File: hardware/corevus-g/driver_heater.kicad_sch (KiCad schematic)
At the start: 4 parts, among them J21 Screw_Terminal_01x02, Q26 60N03F

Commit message: test
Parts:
- R3: value 1kΩ -> 10kΩ
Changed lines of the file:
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@@
       (effects (font (size 0.8 0.8)) (justify right))
     )
-    (property "Value" "1kΩ" (at 63.5 71.12 90)
+    (property "Value" "10kΩ" (at 63.5 71.12 90)
       (effects (font (size 0.8 0.8)))
     )

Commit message: aonteuhasntoidanouidoenuthidntoehuid
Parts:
- Q26: symbol corevus:Q_NMOS-E_Generic_SSSGDDDD -> corevus:NMOS_DFN8
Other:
- moved on the sheet: D1, R3
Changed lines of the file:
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@@
 (kicad_sch (version 20230121) (generator eeschema)
   (paper "User" 140.005 148.006)
-  (junction (at 63.5 60.96) (diameter 0) (color 0 0 0 0)
-  )
-  (wire (pts (xy 63.5 60.96) (xy 63.5 62.23))
+  (junction (at 64.77 59.69) (diameter 0) (color 0 0 0 0)
+  )
+  (wire (pts (xy 64.77 59.69) (xy 64.77 60.96))
     (stroke (width 0) (type default))
   )
@@
     (stroke (width 0) (type default))
   )
-  (wire (pts (xy 63.5 68.58) (xy 63.5 67.31))
-    (stroke (width 0) (type default))
-  )
-  (wire (pts (xy 60.96 60.96) (xy 63.5 60.96))
-    (stroke (width 0) (type default))
-  )
-  (wire (pts (xy 63.5 60.96) (xy 71.12 60.96))
+  (wire (pts (xy 64.77 67.31) (xy 64.77 66.04))
+    (stroke (width 0) (type default))
+  )
+  (wire (pts (xy 62.23 59.69) (xy 64.77 59.69))
+    (stroke (width 0) (type default))
+  )
+  (wire (pts (xy 64.77 59.69) (xy 72.39 59.69))
     (stroke (width 0) (type default))
   )
@@
     (stroke (width 0) (type default))
   )
-  (wire (pts (xy 63.5 74.93) (xy 63.5 73.66))
+  (wire (pts (xy 64.77 73.66) (xy 64.77 72.39))
     (stroke (width 0) (type default))
   )
@@
     (effects (font (size 1.27 1.27)) (justify left bottom))
   )
-  (hierarchical_label "En" (shape input) (at 60.96 60.96 180) (fields_autoplaced)
+  (hierarchical_label "En" (shape input) (at 62.23 59.69 180) (fields_autoplaced)
     (effects (font (size 1.27 1.27)) (justify right))
   )
@@
     )
   )
-  (symbol (lib_id "Device:LED_Small") (at 63.5 64.77 90) (unit 1)
-    (in_bom yes) (on_board yes) (dnp no)
-    (property "Reference" "D1" (at 62.5 63.77 0)
+  (symbol (lib_id "Device:LED_Small") (at 64.77 63.5 90) (unit 1)
+    (in_bom yes) (on_board yes) (dnp no)
+    (property "Reference" "D1" (at 63.77 62.5 0)
       (effects (font (size 0.8 0.8)) (justify left))
     )
-    (property "Value" "Red" (at 62.5 65.77 0)
+    (property "Value" "Red" (at 63.77 64.5 0)
       (effects (font (size 0.8 0.8)) (justify right))
     )
-    (property "Footprint" "AlphaLib:0402LED" (at 63.5 64.77 90)
-      (effects (font (size 1.27 1.27)) hide)
-    )
-    (property "Datasheet" "~" (at 63.5 64.77 90)
+    (property "Footprint" "AlphaLib:0402LED" (at 64.77 63.5 90)
+      (effects (font (size 1.27 1.27)) hide)
+    )
+    (property "Datasheet" "~" (at 64.77 63.5 90)
       (effects (font (size 1.27 1.27)) hide)
     )
@@
     )
   )
-  (symbol (lib_id "power:GND") (at 63.5 74.93 0) (unit 1)
-    (in_bom yes) (on_board yes) (dnp no)
-    (property "Reference" "#PWR0161" (at 63.5 81.28 0)
-      (effects (font (size 1.27 1.27)) hide)
-    )
-    (property "Value" "GND" (at 63.5 77.47 90)
+  (symbol (lib_id "power:GND") (at 64.77 73.66 0) (unit 1)
+    (in_bom yes) (on_board yes) (dnp no)
+    (property "Reference" "#PWR0161" (at 64.77 80.01 0)
+      (effects (font (size 1.27 1.27)) hide)
+    )
+    (property "Value" "GND" (at 64.77 76.2 90)
       (effects (font (size 1.27 1.27)) (justify right) hide)
     )
-    (property "Footprint" "" (at 63.5 74.93 0)
-      (effects (font (size 1.27 1.27)) hide)
-    )
-    (property "Datasheet" "" (at 63.5 74.93 0)
+    (property "Footprint" "" (at 64.77 73.66 0)
+      (effects (font (size 1.27 1.27)) hide)
+    )
+    (property "Datasheet" "" (at 64.77 73.66 0)
       (effects (font (size 1.27 1.27)) hide)
     )
@@
     )
   )
-  (symbol (lib_id "corevus:Q_NMOS-E_Generic_SSSGDDDD") (at 74.93 59.69 0) (unit 1)
-    (in_bom yes) (on_board yes) (dnp no)
-    (property "Reference" "Q26" (at 80.01 58.42 0)
-      (effects (font (size 1.27 1.27)) (justify left))
-    )
-    (property "Value" "60N03F" (at 80.01 60.96 0)
-      (effects (font (size 1.27 1.27)) (justify left))
-    )
-    (property "Footprint" "corevus:MOSFET_DFN8" (at 80.01 57.15 0)
-      (effects (font (size 1.27 1.27)) hide)
-    )
-    (property "Datasheet" "~" (at 74.93 59.69 0)
+  (symbol (lib_id "corevus:NMOS_DFN8") (at 76.2 59.69 0) (unit 1)
+    (in_bom yes) (on_board yes) (dnp no)
+    (property "Reference" "Q26" (at 81.28 58.42 0)
+      (effects (font (size 1.27 1.27)) (justify left))
+    )
+    (property "Value" "60N03F" (at 81.28 60.96 0)
+      (effects (font (size 1.27 1.27)) (justify left))
+    )
+    (property "Footprint" "corevus:MOSFET_DFN8" (at 76.2 76.2 0)
+      (effects (font (size 1.27 1.27)) hide)
+    )
+    (property "Datasheet" "~" (at 76.2 78.74 0)
       (effects (font (size 1.27 1.27)) hide)
     )
@@
     )
   )
-  (symbol (lib_id "Device:R_Small") (at 63.5 71.12 0) (mirror y) (unit 1)
-    (in_bom yes) (on_board yes) (dnp no)
-    (property "Reference" "R3" (at 62.5 73.39 90)
+  (symbol (lib_id "Device:R_Small") (at 64.77 69.85 0) (mirror y) (unit 1)
+    (in_bom yes) (on_board yes) (dnp no)
+    (property "Reference" "R3" (at 63.77 72.12 90)
       (effects (font (size 0.8 0.8)) (justify right))
     )
-    (property "Value" "10kΩ" (at 63.5 71.12 90)
+    (property "Value" "10kΩ" (at 64.77 69.85 90)
       (effects (font (size 0.8 0.8)))
     )
-    (property "Footprint" "AlphaLib:0402R" (at 63.5 71.12 0)
-      (effects (font (size 1.27 1.27)) hide)
-    )
-    (property "Datasheet" "~" (at 63.5 71.12 0)
-      (effects (font (size 1.27 1.27)) hide)
-    )
+    (property "Footprint" "AlphaLib:0402R" (at 64.77 69.85 0)
+      (effects (font (size 1.27 1.27)) hide)
+    )
+    (property "Datasheet" "~" (at 64.77 69.85 0)
+      (effects (font (size 1.27 1.27)) hide)
+    )

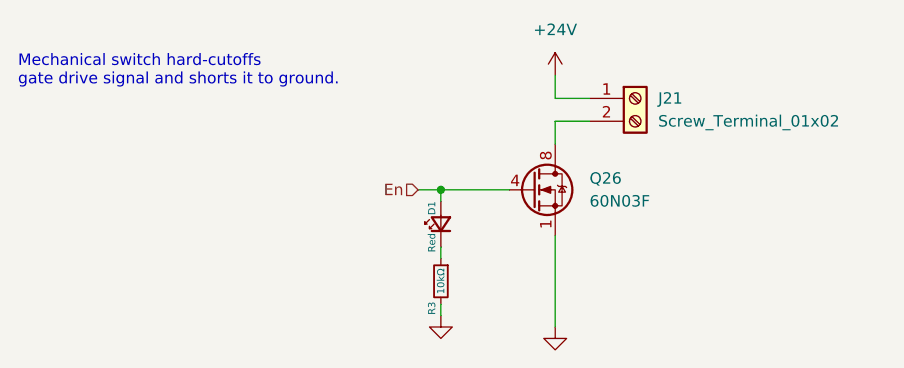
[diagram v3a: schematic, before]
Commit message: version control appears to have magically disappeared the single and dual 2160 driver files :(((((((((, but got some work done on CvG nonetheless
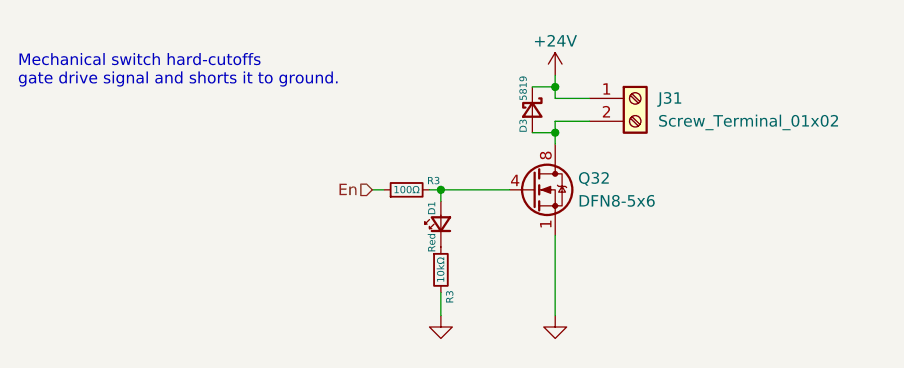
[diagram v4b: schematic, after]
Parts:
- added D3: 5819, Diode_SMD:D_SOD-123, symbol Device:D_Schottky_Small
- added R3: 100Ω, AlphaLib:0402R, symbol Device:R_Small
- J31: renamed from J21; footprint corevus:DB125-3.81-2P -> corevus:DB127V-5.0-2P
- Q32: renamed from Q26; value 60N03F -> DFN8-5x6; footprint corevus:MOSFET_DFN8 -> corevus:MOSFET_DFN8_5x6
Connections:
- net +24V: now also D3.1 (K)
- net En: now also R3.1; no longer D1.2 (A), Q32.4 (G)
- net at J31.2 (Pin_2), Q32.5 (D), Q32.6 (D)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: now also D3.2 (A)
- new net: D1.2 (A), Q32.4 (G), R3.2
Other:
- moved on the sheet: R3

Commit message: v0.4 mostly complete, board needs minor revisions (e.g. pin swap)
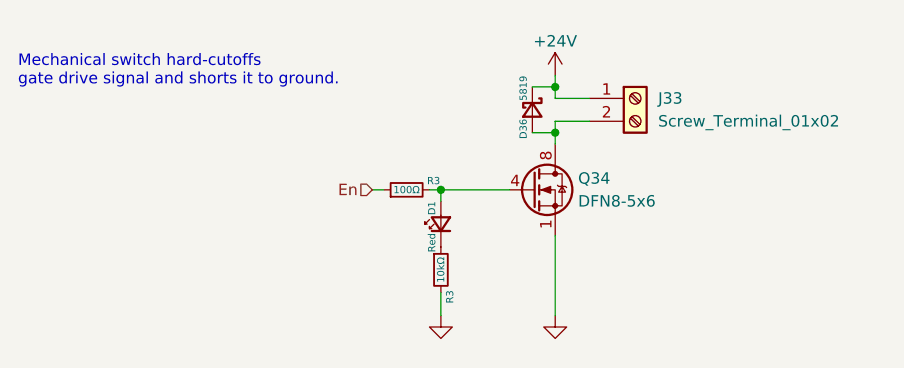
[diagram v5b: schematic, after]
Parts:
- renumbered D3 to D36, J31 to J33, Q32 to Q34
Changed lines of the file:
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@@
   (symbol (lib_id "Connector:Screw_Terminal_01x02") (at 86.36 49.53 0) (unit 1)
     (in_bom yes) (on_board yes) (dnp no)
-    (property "Reference" "J31" (at 88.9 49.53 0)
+    (property "Reference" "J33" (at 88.9 49.53 0)
       (effects (font (size 1.27 1.27)) (justify left))
     )
@@
     (instances
       (project "corevus-g"
-        (path "/1a565782-f217-442e-b118-196625f31c53/e431a135-0fb4-461f-9017-9bc2d88ea1f7"
-          (reference "J31") (unit 1)
-        )
         (path "/1a565782-f217-442e-b118-196625f31c53/a01cd58f-7f75-4e1a-8889-9711b3d0cced"
           (reference "J33") (unit 1)
@@
       )
       (project "corevus-g"
-        (path "/1a565782-f217-442e-b118-196625f31c53"
-          (reference "R76") (unit 1)
-        )
-        (path "/1a565782-f217-442e-b118-196625f31c53/e431a135-0fb4-461f-9017-9bc2d88ea1f7"
-          (reference "R121") (unit 1)
-        )
         (path "/1a565782-f217-442e-b118-196625f31c53/a01cd58f-7f75-4e1a-8889-9711b3d0cced"
           (reference "R123") (unit 1)
@@
   (symbol (lib_id "power:GND") (at 77.47 73.66 0) (unit 1)
     (in_bom yes) (on_board yes) (dnp no)
-    (property "Reference" "#PWR0118" (at 77.47 80.01 0)
+    (property "Reference" "#PWR065" (at 77.47 80.01 0)
       (effects (font (size 1.27 1.27)) hide)
     )
@@
     (instances
       (project "corevus-g"
-        (path "/1a565782-f217-442e-b118-196625f31c53"
-          (reference "#PWR0118") (unit 1)
-        )
-        (path "/1a565782-f217-442e-b118-196625f31c53/e431a135-0fb4-461f-9017-9bc2d88ea1f7"
-          (reference "#PWR050") (unit 1)
-        )
         (path "/1a565782-f217-442e-b118-196625f31c53/a01cd58f-7f75-4e1a-8889-9711b3d0cced"
           (reference "#PWR065") (unit 1)
@@
   (symbol (lib_id "power:+24V") (at 77.47 46.99 0) (unit 1)
     (in_bom yes) (on_board yes) (dnp no)
-    (property "Reference" "#PWR049" (at 77.47 50.8 0)
+    (property "Reference" "#PWR064" (at 77.47 50.8 0)
       (effects (font (size 1.27 1.27)) hide)
     )
@@
     (instances
       (project "corevus-g"
-        (path "/1a565782-f217-442e-b118-196625f31c53/e431a135-0fb4-461f-9017-9bc2d88ea1f7"
-          (reference "#PWR049") (unit 1)
-        )
         (path "/1a565782-f217-442e-b118-196625f31c53/a01cd58f-7f75-4e1a-8889-9711b3d0cced"
           (reference "#PWR064") (unit 1)
@@
       )
       (project "corevus-g"
-        (path "/1a565782-f217-442e-b118-196625f31c53"
-          (reference "D18") (unit 1)
-        )
-        (path "/1a565782-f217-442e-b118-196625f31c53/e431a135-0fb4-461f-9017-9bc2d88ea1f7"
-          (reference "D32") (unit 1)
-        )
         (path "/1a565782-f217-442e-b118-196625f31c53/a01cd58f-7f75-4e1a-8889-9711b3d0cced"
           (reference "D34") (unit 1)
@@
   (symbol (lib_id "Device:D_Schottky_Small") (at 74.93 50.8 270) (unit 1)
     (in_bom yes) (on_board yes) (dnp no)
-    (property "Reference" "D3" (at 73.93 51.8 0)
+    (property "Reference" "D36" (at 73.93 51.8 0)
       (effects (font (size 0.8 0.8)) (justify left))
     )
@@
     (instances
       (project "corevus-g"
-        (path "/1a565782-f217-442e-b118-196625f31c53"
-          (reference "D3") (unit 1)
-        )
         (path "/1a565782-f217-442e-b118-196625f31c53/bb16317b-ca89-4c54-91fa-fbae4a7551b1"
           (reference "D36") (unit 1)
         )
-        (path "/1a565782-f217-442e-b118-196625f31c53/e431a135-0fb4-461f-9017-9bc2d88ea1f7"
-          (reference "D37") (unit 1)
-        )
         (path "/1a565782-f217-442e-b118-196625f31c53/8e27c19c-e19c-4813-a1cf-aa58793105a1"
           (reference "D38") (unit 1)
@@
   (symbol (lib_id "power:GND") (at 64.77 73.66 0) (unit 1)
     (in_bom yes) (on_board yes) (dnp no)
-    (property "Reference" "#PWR0161" (at 64.77 80.01 0)
+    (property "Reference" "#PWR063" (at 64.77 80.01 0)
       (effects (font (size 1.27 1.27)) hide)
     )
@@
     (instances
       (project "corevus-g"
-        (path "/1a565782-f217-442e-b118-196625f31c53"
-          (reference "#PWR0161") (unit 1)
-        )
-        (path "/1a565782-f217-442e-b118-196625f31c53/e431a135-0fb4-461f-9017-9bc2d88ea1f7"
-          (reference "#PWR048") (unit 1)
-        )
         (path "/1a565782-f217-442e-b118-196625f31c53/a01cd58f-7f75-4e1a-8889-9711b3d0cced"
           (reference "#PWR063") (unit 1)
@@
   (symbol (lib_id "corevus:NMOS_DFN8") (at 76.2 59.69 0) (unit 1)
     (in_bom yes) (on_board yes) (dnp no)
-    (property "Reference" "Q32" (at 80.01 58.42 0)
+    (property "Reference" "Q34" (at 80.01 58.42 0)
       (effects (font (size 1.27 1.27)) (justify left))
     )
@@
     (instances
       (project "corevus-g"
-        (path "/1a565782-f217-442e-b118-196625f31c53/e431a135-0fb4-461f-9017-9bc2d88ea1f7"
-          (reference "Q32") (unit 1)
-        )
         (path "/1a565782-f217-442e-b118-196625f31c53/a01cd58f-7f75-4e1a-8889-9711b3d0cced"
           (reference "Q34") (unit 1)
@@
       )
       (project "corevus-g"
-        (path "/1a565782-f217-442e-b118-196625f31c53"
-          (reference "R76") (unit 1)
-        )
-        (path "/1a565782-f217-442e-b118-196625f31c53/e431a135-0fb4-461f-9017-9bc2d88ea1f7"
-          (reference "R114") (unit 1)
-        )
         (path "/1a565782-f217-442e-b118-196625f31c53/a01cd58f-7f75-4e1a-8889-9711b3d0cced"
           (reference "R116") (unit 1)

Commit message: non-working commit, moved around various connectors etc in preparation for v0.5
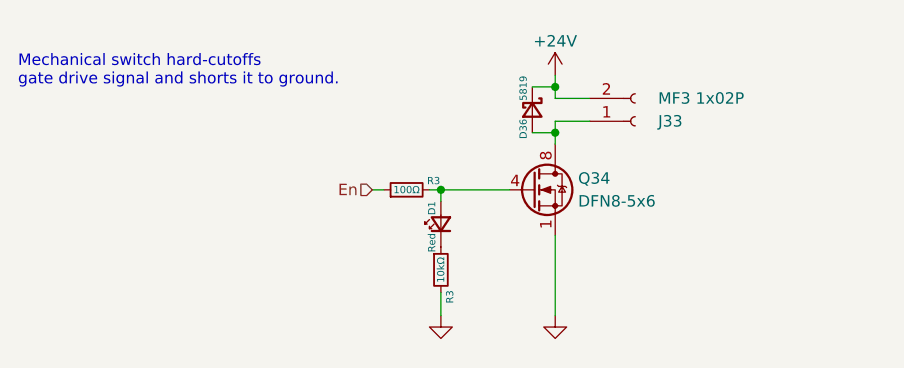
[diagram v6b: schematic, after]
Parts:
- J33: value Screw_Terminal_01x02 -> MF3 1x02P; footprint corevus:DB127V-5.0-2P -> corevus:XKB_X3025WR-02; symbol Connector:Screw_Terminal_01x02 -> Connector:Conn_01x02_Socket
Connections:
- net +24V: now also J33.2 (Pin_2); no longer J33.1 (Pin_1)
- net at D36.2 (A), Q34.5 (D), Q34.6 (D)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: now also J33.1 (Pin_1); no longer J33.2 (Pin_2)
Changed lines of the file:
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@@
     (effects (font (size 1.27 1.27)) (justify right))
   )
-  (symbol (lib_id "Connector:Screw_Terminal_01x02") (at 86.36 49.53 0) (unit 1)
+  (symbol (lib_id "Connector:Conn_01x02_Socket") (at 86.36 52.07 0) (mirror x) (unit 1)
     (in_bom yes) (on_board yes) (dnp no)
-    (property "Reference" "J33" (at 88.9 49.53 0)
+    (property "Reference" "J33" (at 88.9 52.07 0)
       (effects (font (size 1.27 1.27)) (justify left))
     )
-    (property "Value" "Screw_Terminal_01x02" (at 88.9 52.07 0)
+    (property "Value" "MF3 1x02P" (at 88.9 49.53 0)
       (effects (font (size 1.27 1.27)) (justify left))
     )
-    (property "Footprint" "corevus:DB127V-5.0-2P" (at 86.36 49.53 0)
+    (property "Footprint" "corevus:XKB_X3025WR-02" (at 86.36 52.07 0)
       (effects (font (size 1.27 1.27)) hide)
     )
-    (property "Datasheet" "~" (at 86.36 49.53 0)
+    (property "Datasheet" "~" (at 86.36 52.07 0)
       (effects (font (size 1.27 1.27)) hide)
     )

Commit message: why not
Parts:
- J33: footprint corevus:XKB_X3025WR-02 -> corevus:HCTL_HC-MX3.0-2A
- R3: value 10kΩ -> 22kΩ
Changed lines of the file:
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@@
 			)
 		)
-		(property "Footprint" "corevus:XKB_X3025WR-02"
+		(property "Footprint" "corevus:HCTL_HC-MX3.0-2A"
 			(at 86.36 52.07 0)
 			(effects
@@
 			)
 		)
-		(property "Value" "10kΩ"
+		(property "Value" "22kΩ"
 			(at 64.77 68.58 90)
 			(effects
